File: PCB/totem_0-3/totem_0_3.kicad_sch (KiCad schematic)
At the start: 88 parts, among them J1 MJ-4PP-9, J2 MJ-4PP-9, U1 xiao-ble, U2 xiao-ble

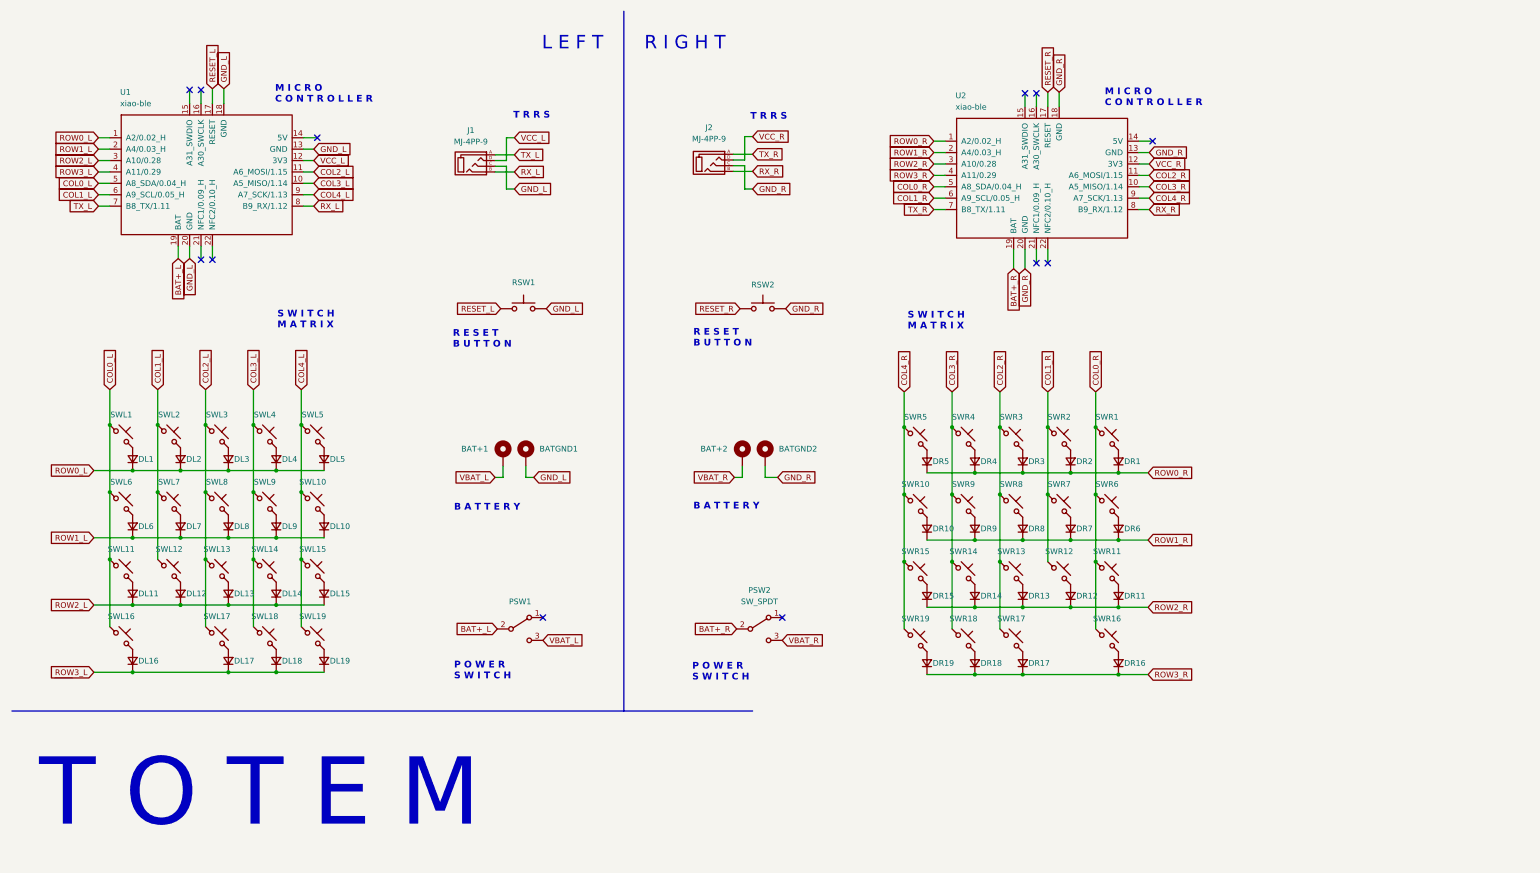
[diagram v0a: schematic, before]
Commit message: optimising for manifacturability at jlc pcb, seperating connectors from switch footprint
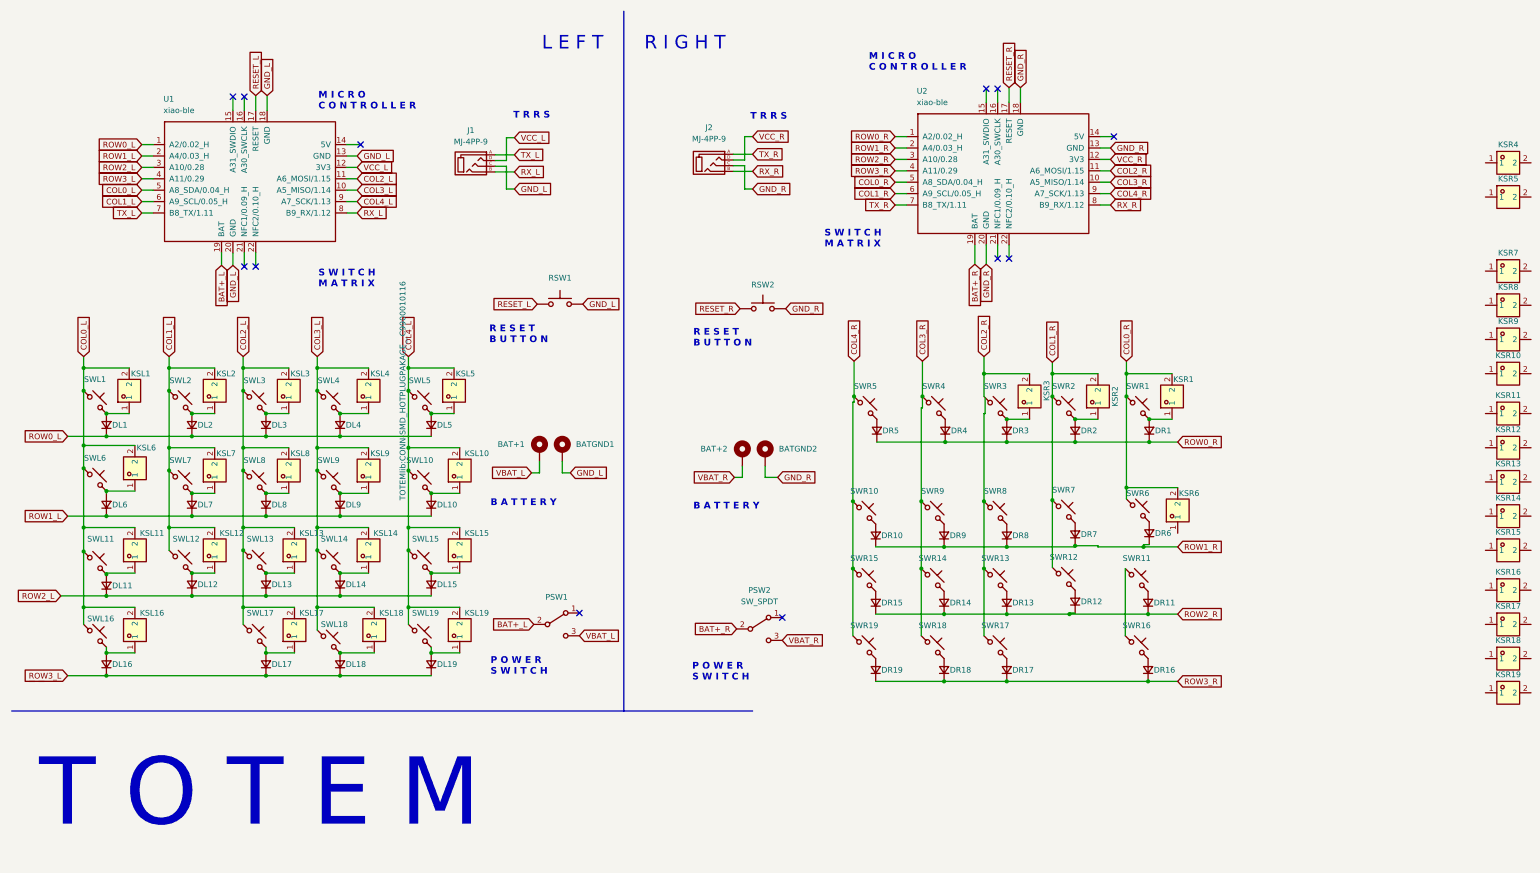
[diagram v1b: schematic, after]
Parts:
- added KSL1, KSL10, KSL11, KSL12, KSL13, KSL14, KSL15, KSL16, KSL17, KSL18, KSL19, KSL2, KSL3, KSL4, KSL5, KSL6, KSL7, KSL8, KSL9, KSR1, KSR10, KSR11, KSR12, KSR13, KSR14, KSR15, KSR16, KSR17, KSR18, KSR19, KSR2, KSR3, KSR4, KSR5, KSR6, KSR7, KSR8, KSR9: CPG135001S30, TOTEMlib:CONN-SMD_HOTPLUGPAKAGE__C9900010116, symbol Totem_lib:CPG135001S30
- BAT+1, BAT+2, BATGND1, BATGND2, SWL1, SWL10, SWL11, SWL12, SWL13, SWL14, SWL15, SWL16, SWL17, SWL18, SWL19, SWL2, SWL3, SWL4, SWL5, SWL6, SWL7, SWL8, SWL9, SWR1, SWR10, SWR11, SWR12, SWR13, SWR14, SWR15, SWR16, SWR17, SWR18, SWR19, SWR2, SWR3, SWR4, SWR5, SWR6, SWR7, SWR8, SWR9, U1, U2: now left out of the parts list
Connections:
- net COL0_L: now also KSL1.2, KSL11.2, KSL16.2, KSL6.2
- net COL0_R: now also KSR1.2, KSR6.2; no longer SWR11.1, SWR16.1
- net COL1_L: now also KSL12.2, KSL2.2, KSL7.2
- net COL1_R: now also KSR2.2
- net COL2_L: now also KSL13.2, KSL17.2, KSL3.2, KSL8.2
- net COL2_R: now also KSR3.2; no longer SWR13.1, SWR17.1, SWR8.1
- net COL3_L: now also KSL14.2, KSL18.2, KSL4.2, KSL9.2
- net COL4_L: now also KSL10.2, KSL15.2, KSL19.2, KSL5.2
- net at DL19.2 (A), SWL19.2: now also KSL19.1
- net at DR2.2 (A), SWR2.2: now also KSR2.1
- net at DL17.2 (A), SWL17.2: now also KSL17.1
- net at DL16.2 (A), SWL16.2: now also KSL16.1
- net at DL4.2 (A), SWL4.2: now also KSL4.1
- net at DR3.2 (A), SWR3.2: now also KSR3.1
- net at DL3.2 (A), SWL3.2: now also KSL3.1
- net at DL7.2 (A), SWL7.2: now also KSL7.1
- net at DL1.2 (A), SWL1.2: now also KSL1.1
- net at DL2.2 (A), SWL2.2: now also KSL2.1
- net at DL8.2 (A), SWL8.2: now also KSL8.1
- net at DL14.2 (A), SWL14.2: now also KSL14.1
- net at DL5.2 (A), SWL5.2: now also KSL5.1
- net at DL9.2 (A), SWL9.2: now also KSL9.1
- net at DL10.2 (A), SWL10.2: now also KSL10.1
- net at DL18.2 (A), SWL18.2: now also KSL18.1
- net at DL15.2 (A), SWL15.2: now also KSL15.1
- net at DL13.2 (A), SWL13.2: now also KSL13.1
- net at DR1.2 (A), SWR1.2: now also KSR1.1
- net at DL6.2 (A), SWL6.2: now also KSL6.1
- net at DL11.2 (A), SWL11.2: now also KSL11.1
- net at DL12.2 (A), SWL12.2: now also KSL12.1
- new net: SWR11.1, SWR16.1
- new net: SWR13.1, SWR17.1, SWR8.1
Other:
- moved on the sheet: BAT+1, BATGND1, DL1, DL10, DL11, DL12, DL13, DL14, DL15, DL16, DL17, DL18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

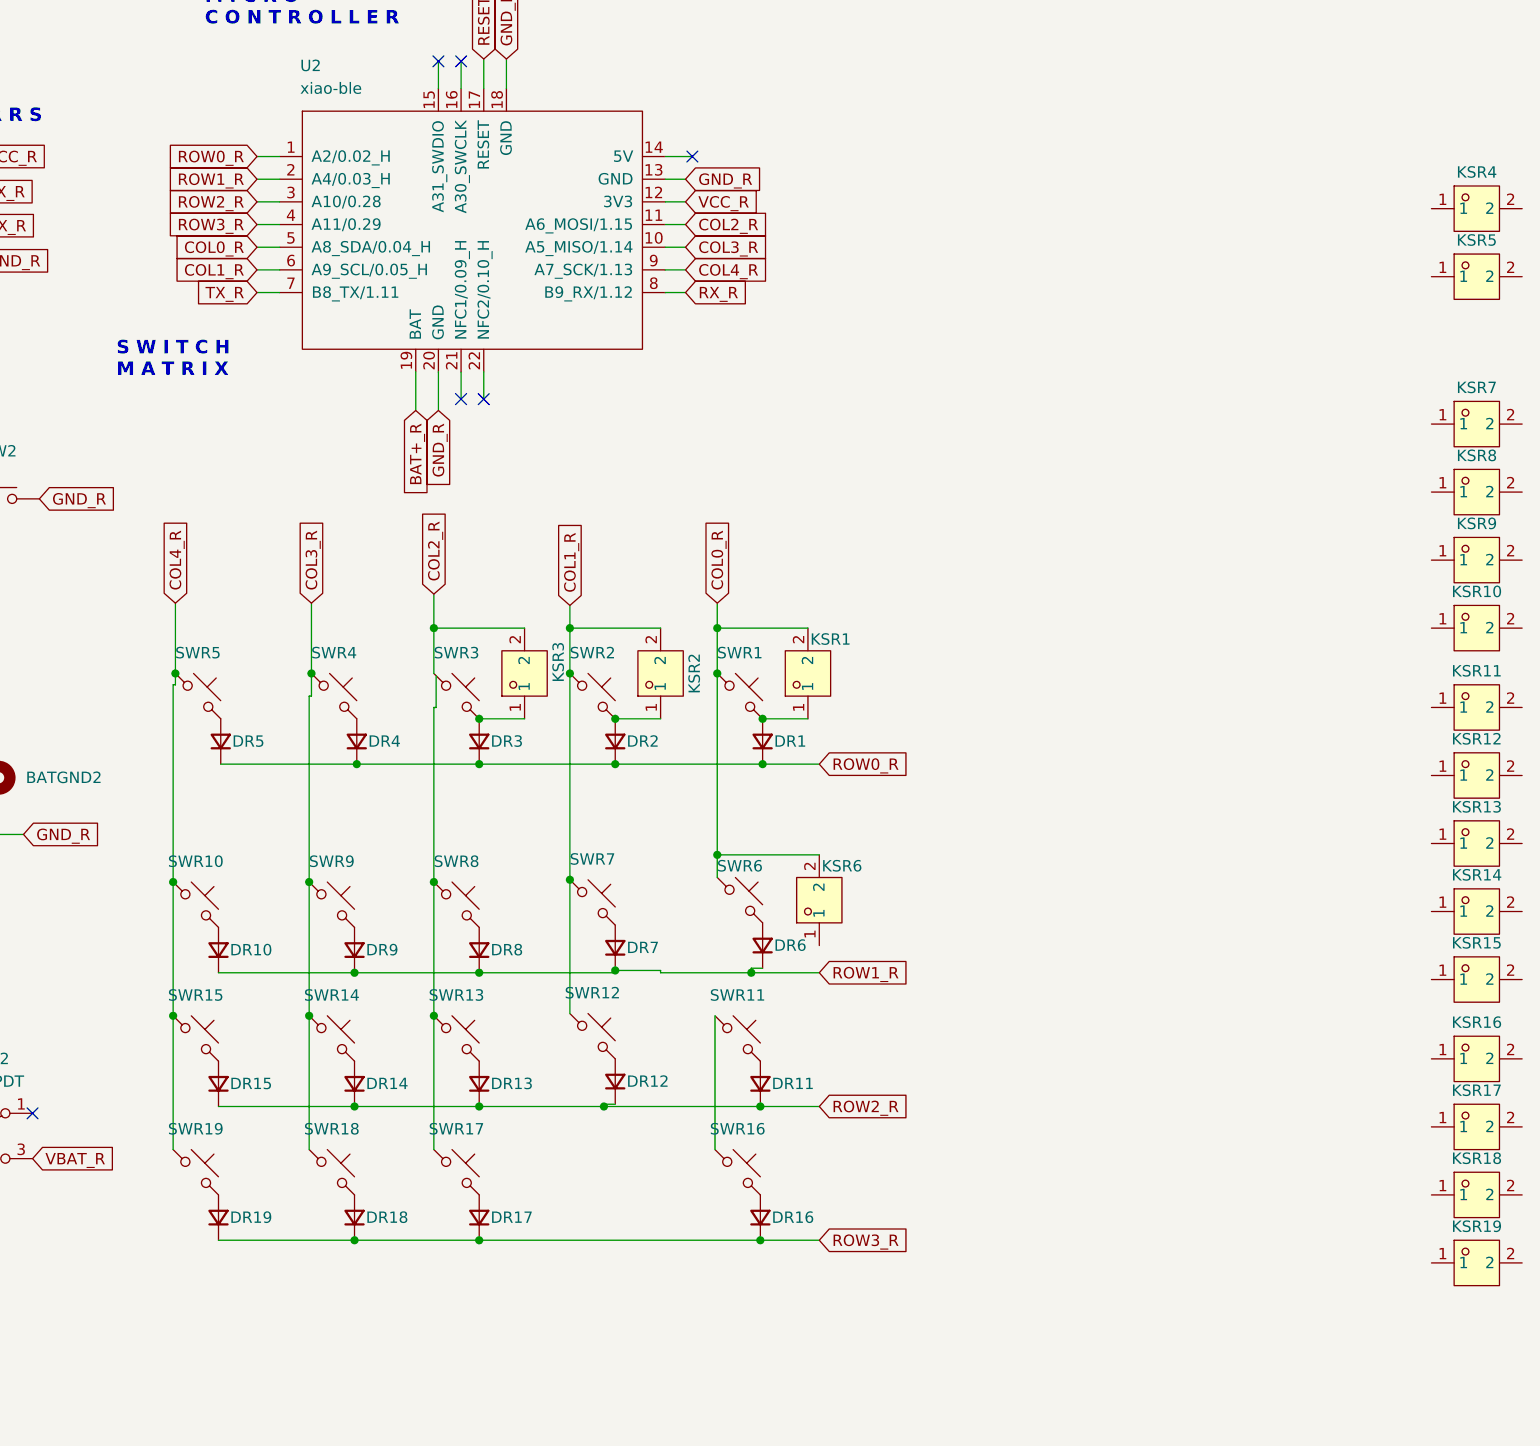
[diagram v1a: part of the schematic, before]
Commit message: finished adding switch sockets in the original positions
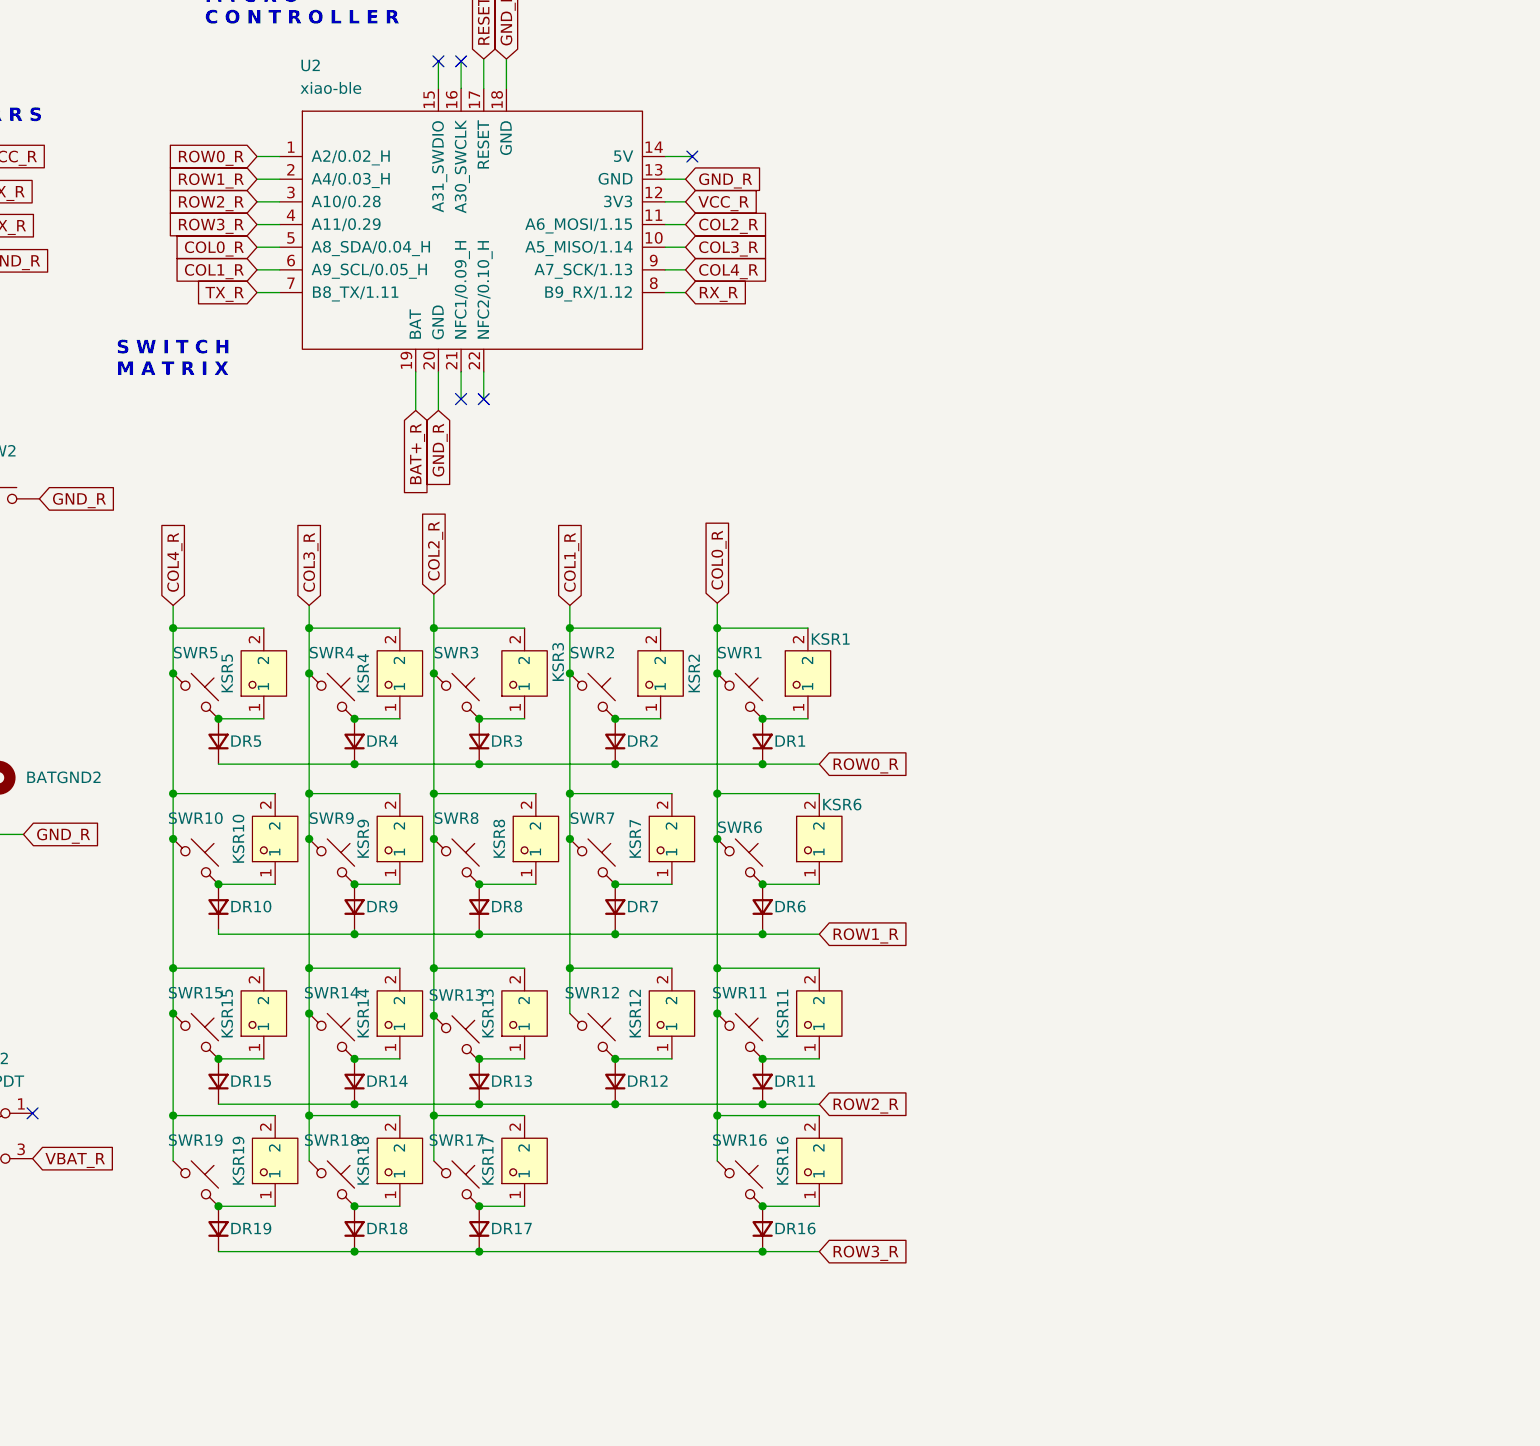
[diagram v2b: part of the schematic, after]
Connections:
- net COL0_R: now also KSR11.2, KSR16.2, SWR11.1, SWR16.1
- net COL1_R: now also KSR12.2, KSR7.2
- net COL2_R: now also KSR13.2, KSR17.2, KSR8.2, SWR13.1, SWR17.1, SWR8.1
- net COL3_R: now also KSR14.2, KSR18.2, KSR4.2, KSR9.2
- net COL4_R: now also KSR10.2, KSR15.2, KSR19.2, KSR5.2
- net at KSR9.1: now also DR9.2 (A), SWR9.2
- net at DR16.2 (A), SWR16.2: now also KSR16.1
- net at DR6.2 (A), SWR6.2: now also KSR6.1
- net at DR5.2 (A), SWR5.2: now also KSR5.1
- net at KSR10.1: now also DR10.2 (A), SWR10.2
- net at DR12.2 (A), SWR12.2: now also KSR12.1
- net at KSR7.1: now also DR7.2 (A), SWR7.2
- net at KSR14.1: now also DR14.2 (A), SWR14.2
- net at DR8.2 (A), SWR8.2: now also KSR8.1
- net at DR13.2 (A), SWR13.2: now also KSR13.1
- net at KSR11.1: now also DR11.2 (A), SWR11.2
- net at DR15.2 (A), SWR15.2: now also KSR15.1
- net at DR19.2 (A), SWR19.2: now also KSR19.1
- net at KSR4.1: now also DR4.2 (A), SWR4.2
- net at DR17.2 (A), SWR17.2: now also KSR17.1
- net at DR18.2 (A), SWR18.2: now also KSR18.1
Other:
- moved on the sheet: DR10, DR16, DR17, DR18, DR19, DR6, DR7, DR8, DR9, KSR10, KSR11, KSR12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
